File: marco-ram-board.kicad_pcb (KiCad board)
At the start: 4 copper layers, 160 x 100 mm, 186 parts, among them J201 PRG_USB, J202 MCU_RST, J203 MCU_BOOT0, J204 FT_TXD, J205 FT_RXD, J206 CONN_JTAG, J301 CONN_MCU_SERIAL, J302 CONN_EXT, J501 MCU_USB, J502 SD_Card, J503 CONN_DISP, J504 RJ45_Amphenol_RJMG1BD3B8K1ANR, J601 CONN_JACK_12V, J602 CONN_SCREW_12V, Q201 MMBT3906, Q601 DMP3037LSS, SW301 SW_RST, SW302 SW_BOOT0, SW501 BTN0, SW502 BTN1, SW503 BTN2, SW504 BTN3, SW601 PWR_SW, U201 FT2232HL, U301 STM32F765IITx, U401 IS42S86400D, U402 IS42S86400D, U403 IS42S86400D, U404 IS42S86400D, U405 IS42S86400D, U406 IS42S86400D, U407 IS42S86400D, U408 IS42S86400D, U501 KSZ8081RNA, U601 LM2576S-3.3, Y201 12MHz, Y301 25MHz

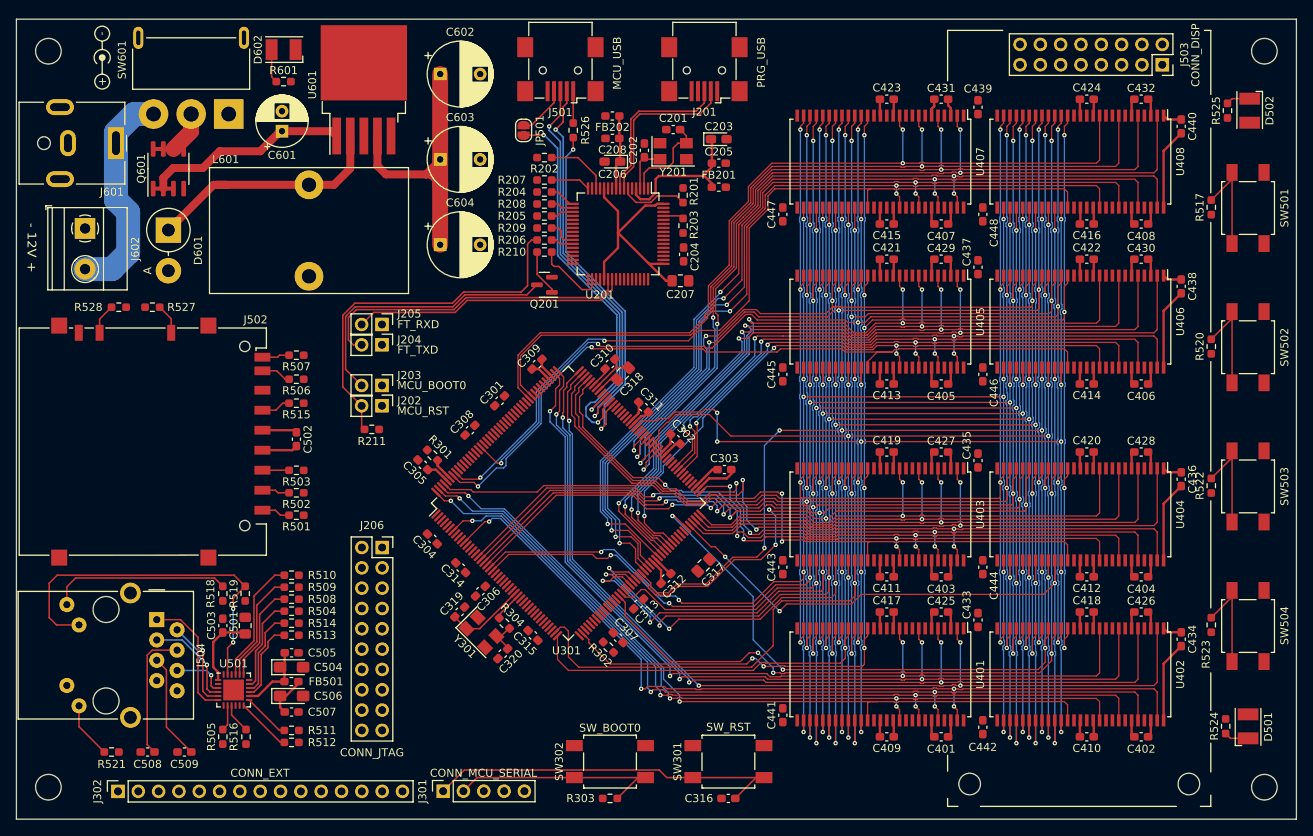
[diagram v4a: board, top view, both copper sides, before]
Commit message: More SDRAM routing cleanup, partial screen/buttons routing
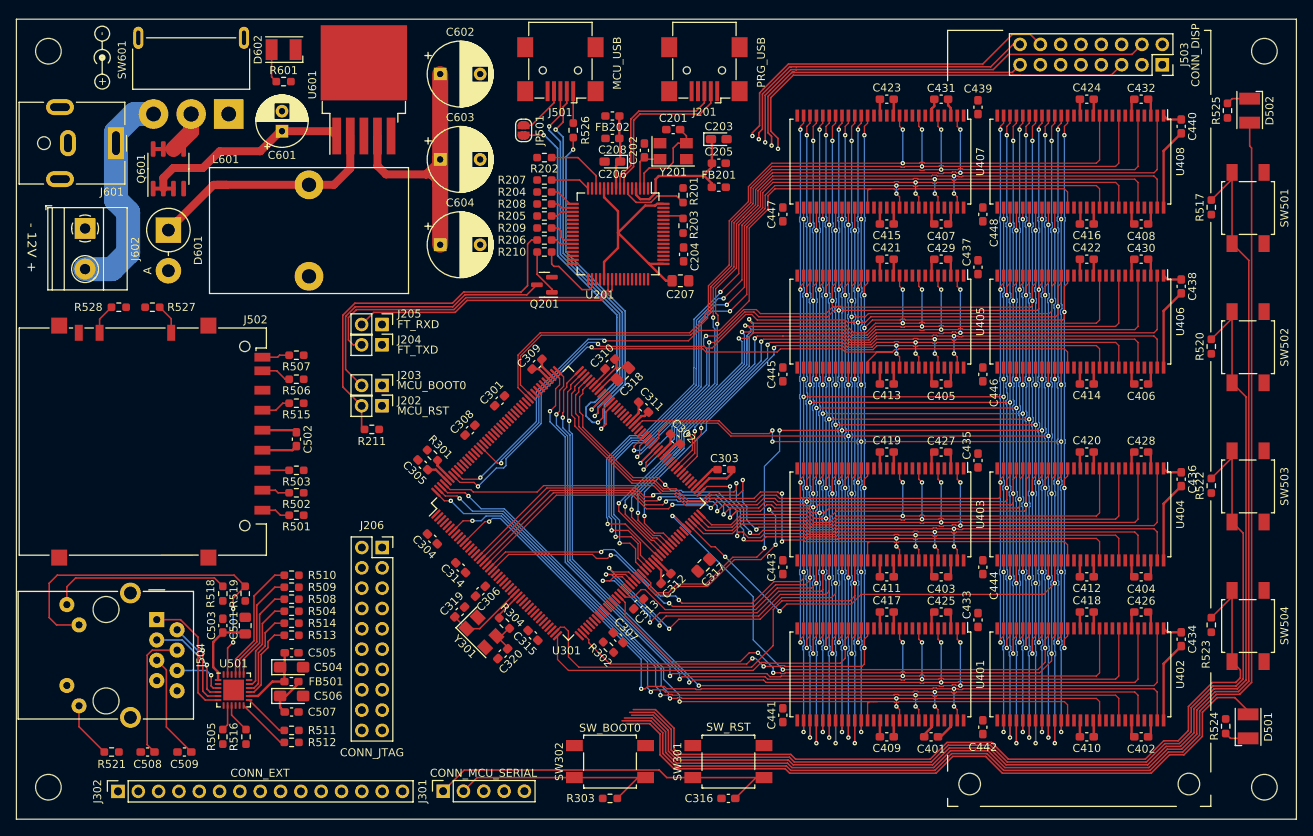
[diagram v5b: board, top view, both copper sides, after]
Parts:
- moved C401 1.26 mm to (184.3, 129.7)
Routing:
- net /mcu-if/LED1: track 0.00 -> 160.9 mm
- net /mcu-if/BTN0: track 12.6 -> 158.2 mm
- net /mcu-if/BTN1: track 12.6 -> 139.2 mm
- net /mcu-if/BTN2: track 12.6 -> 121.3 mm
- net /mcu-if/LED0: track 0.00 -> 90.4 mm
- net /mcu-if/BTN3: track 12.6 -> 102.7 mm
- net /mcu-if/DISP.SCLK: track 0.00 -> 55.7 mm, vias 0 -> 1
- net /mcu-if/DISP.MOSI: track 0.00 -> 53.3 mm, vias 0 -> 1
- net /mcu-if/DISP.DC: track 0.00 -> 44.4 mm, vias 0 -> 1
- net /mcu-if/DISP.CS: track 0.00 -> 41.1 mm, vias 0 -> 1
- net /mcu-if/DISP.~{RST}: track 0.00 -> 39.8 mm, vias 0 -> 1
- net /mcu/SDRAM.D10: track 97.1 -> 100.4 mm
- net /mcu/SDRAM.CLK: track 200.2 -> 198.1 mm
- net /mcu/SDRAM.A12: track 199.2 -> 198.2 mm
- net /mcu/SDRAM.D14: track 76.1 -> 75.3 mm
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
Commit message: Screen/buttons/LEDs routing
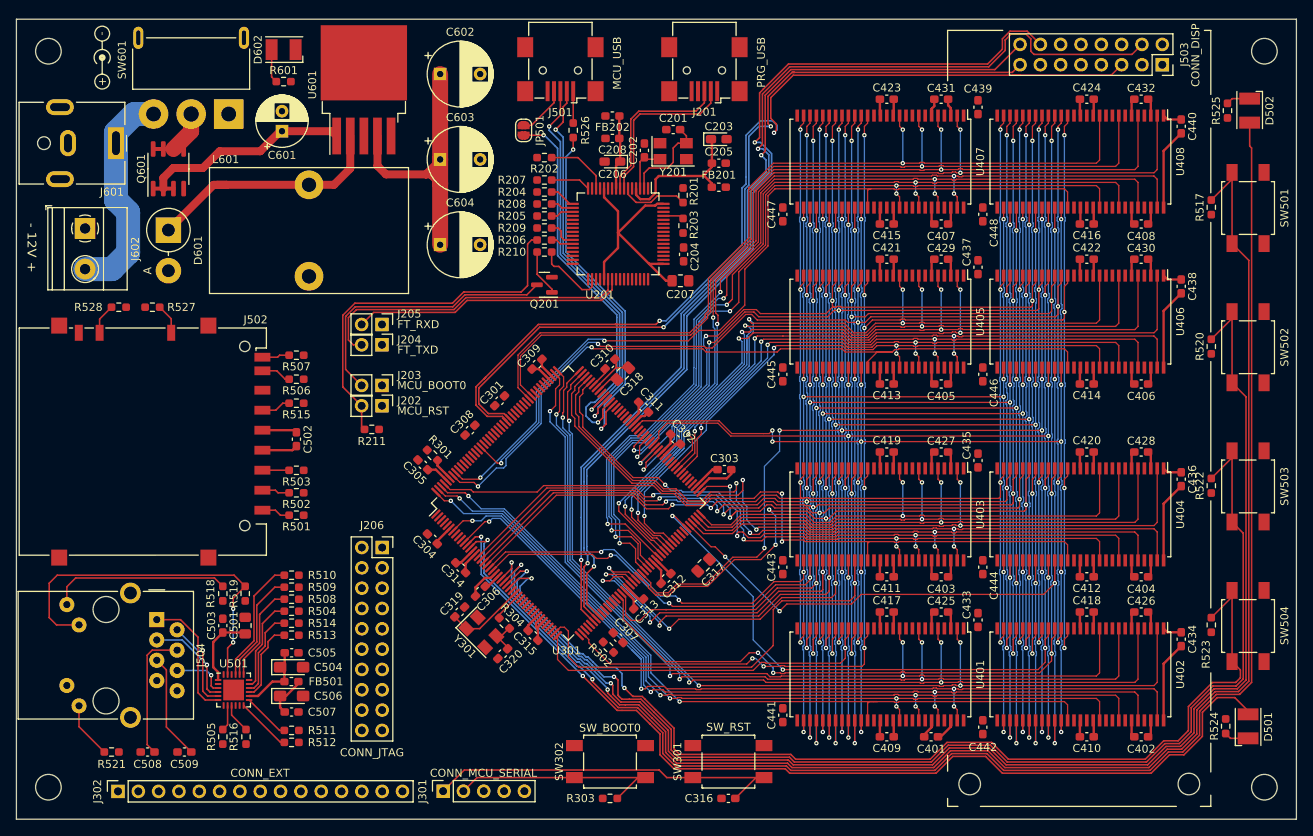
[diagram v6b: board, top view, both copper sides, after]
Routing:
- net /mcu-if/DISP.SCLK: track 55.7 -> 131.1 mm, vias 1 -> 2
- net /mcu-if/DISP.DC: track 44.4 -> 117.6 mm, vias 1 -> 2
- net /mcu-if/DISP.CS: track 41.1 -> 110.9 mm, vias 1 -> 2
- net /mcu-if/DISP.MOSI: track 53.3 -> 119.5 mm, vias 1 -> 2
- net /mcu-if/DISP.~{RST}: track 39.8 -> 101.7 mm, vias 1 -> 2
- net /mcu-if/LED0: track 90.4 -> 123.1 mm, vias 0 -> 2
- net /mcu-if/LED1: track 160.9 -> 193.0 mm, vias 0 -> 2
- net /mcu-if/BTN1: track 139.2 -> 168.0 mm, vias 0 -> 2
- net /mcu-if/BTN2: track 121.3 -> 149.3 mm, vias 0 -> 2
- net /mcu-if/BTN0: track 158.2 -> 185.9 mm, vias 0 -> 2
- net /mcu-if/BTN3: track 102.7 -> 129.8 mm, vias 0 -> 2
- net VDD: track 146.3 -> 161.9 mm
- net GND: track 135.1 -> 147.2 mm
- net /mcu/SDRAM.A6: track 201.0 -> 203.5 mm
- net /mcu/SDRAM.D31: track 107.0 -> 108.9 mm
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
